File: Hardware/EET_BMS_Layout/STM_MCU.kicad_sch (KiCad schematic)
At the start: 82 parts, among them J10 SW_Debug_Connector, J12 Conn_02x20_Odd_Even, J13 PWM, J5 Display, J6 RS485, J8 UART_Shell, J9 Power_In, U10 LF33_TO220, U2 INA181, U2 STISO621, U4 ISO1500, U5 LF33_TO220, U6 STM32H755ZITx, U9 STM32L031F6Px, Y1 16Mhz

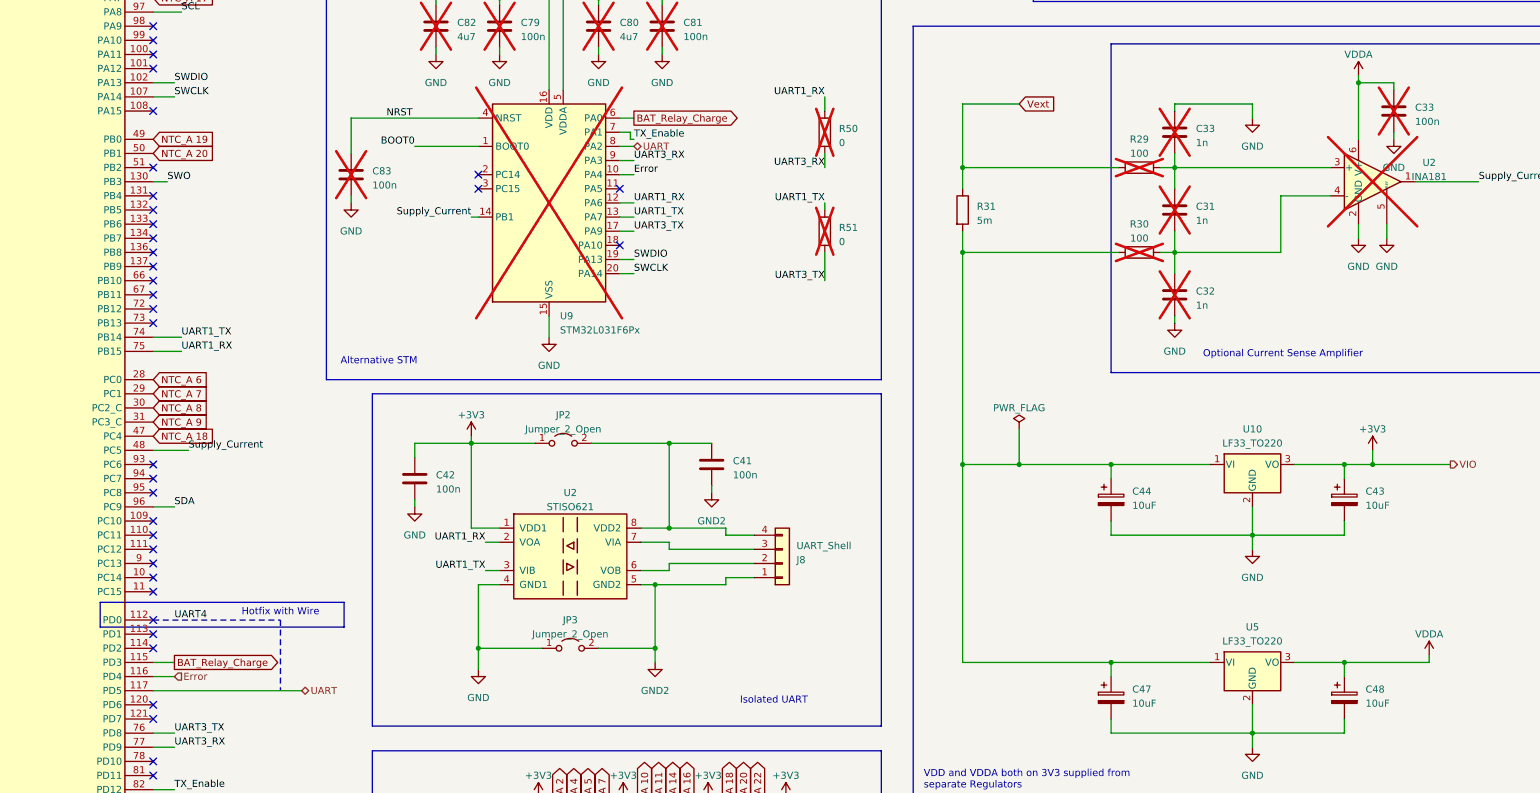
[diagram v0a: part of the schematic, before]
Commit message: fixed a bug in the firmware. Added in Hardware documentation
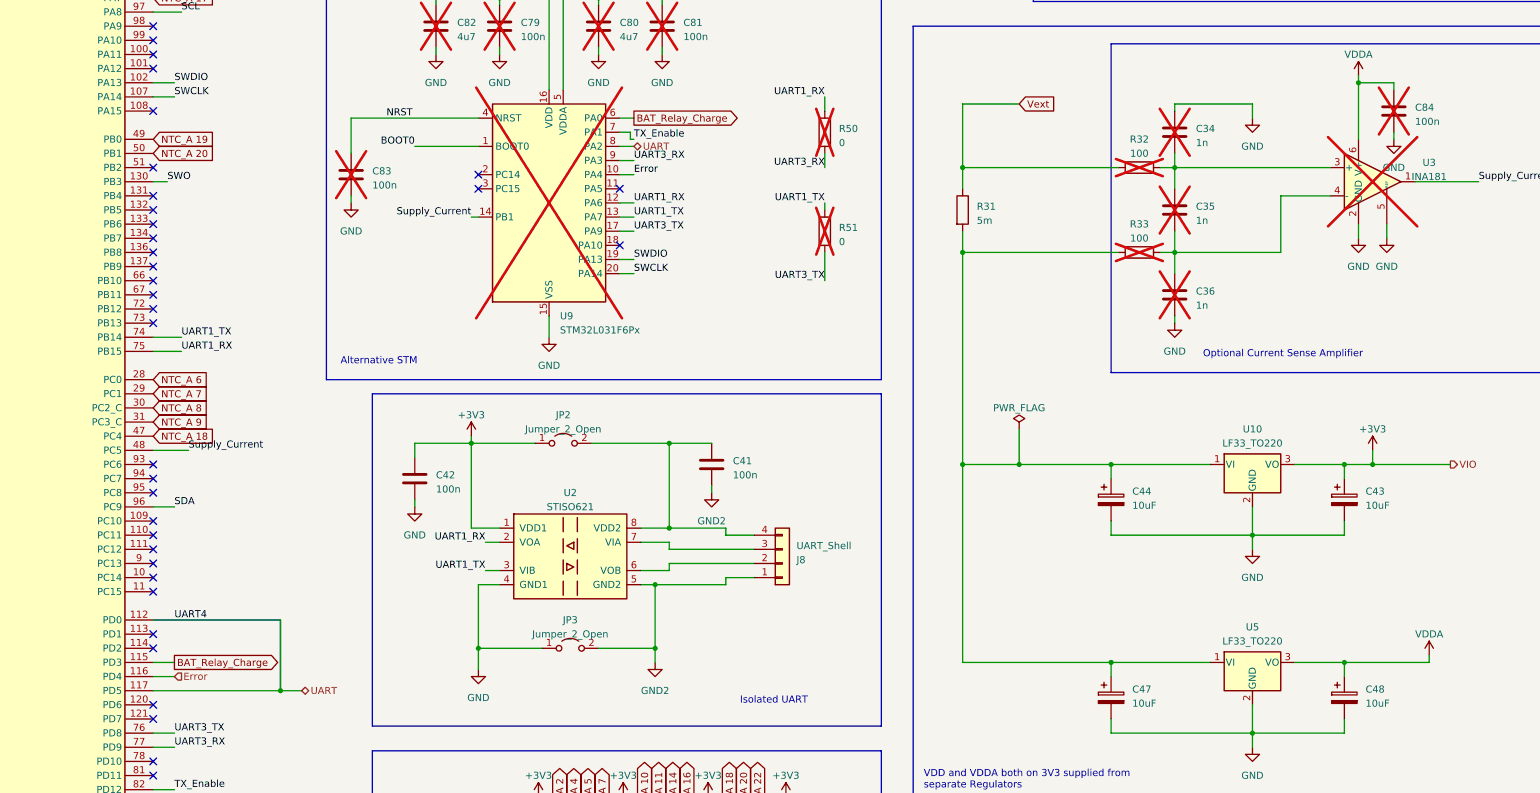
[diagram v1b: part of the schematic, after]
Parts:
- renumbered C33 to C34, C31 to C35, C32 to C36, C33 to C84, R29 to R32, R30 to R33, U2 to U3
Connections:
- net UART: now also U6.112 (PD0)
- no-connect marks 64 -> 63
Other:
- note removed: "Hotfix with Wire"
